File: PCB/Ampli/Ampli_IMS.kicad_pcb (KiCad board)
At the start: 2 copper layers, 65 x 32 mm, 22 parts, among them J1 5227161-3, J2 5227161-3, J3 Conn_01x03_Male, SW1 SS22D0205G2, U1 ADA4625-1, U2 LT1464CS8

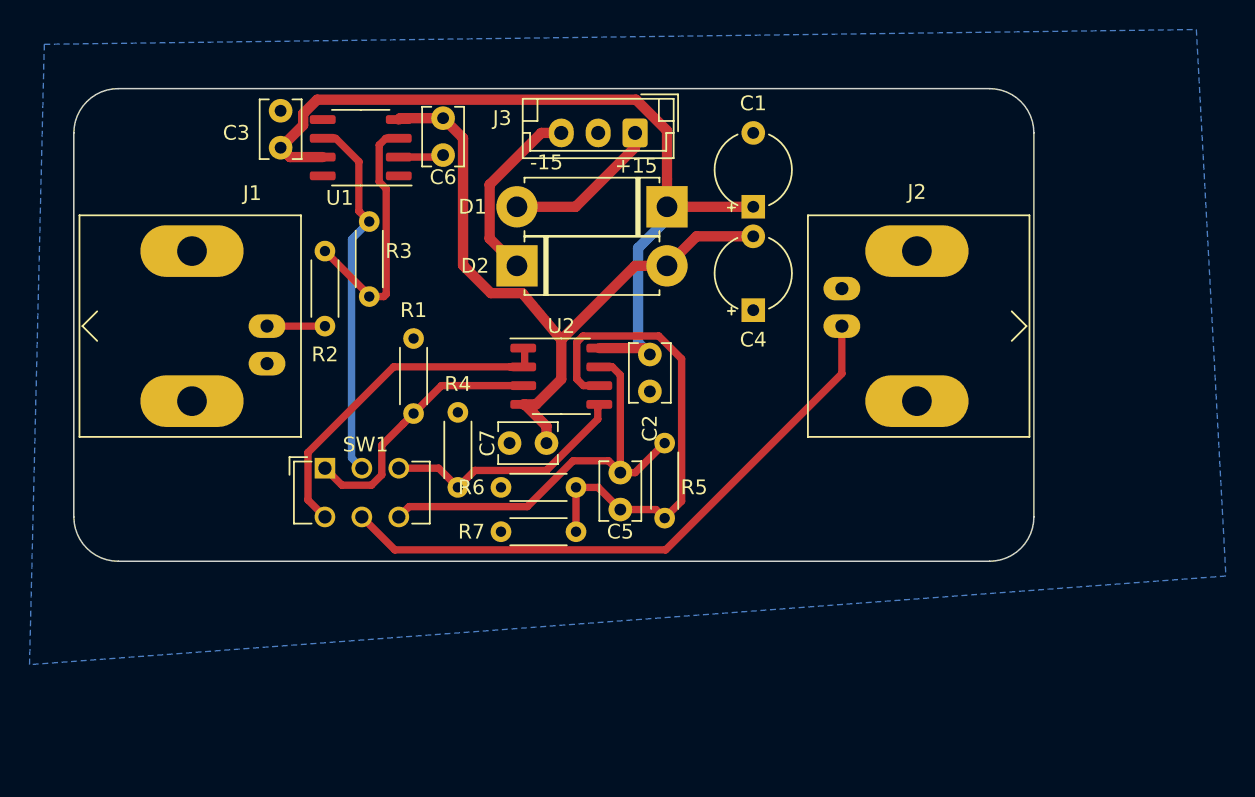
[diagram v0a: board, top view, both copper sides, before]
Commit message: Signal tracks enlarged
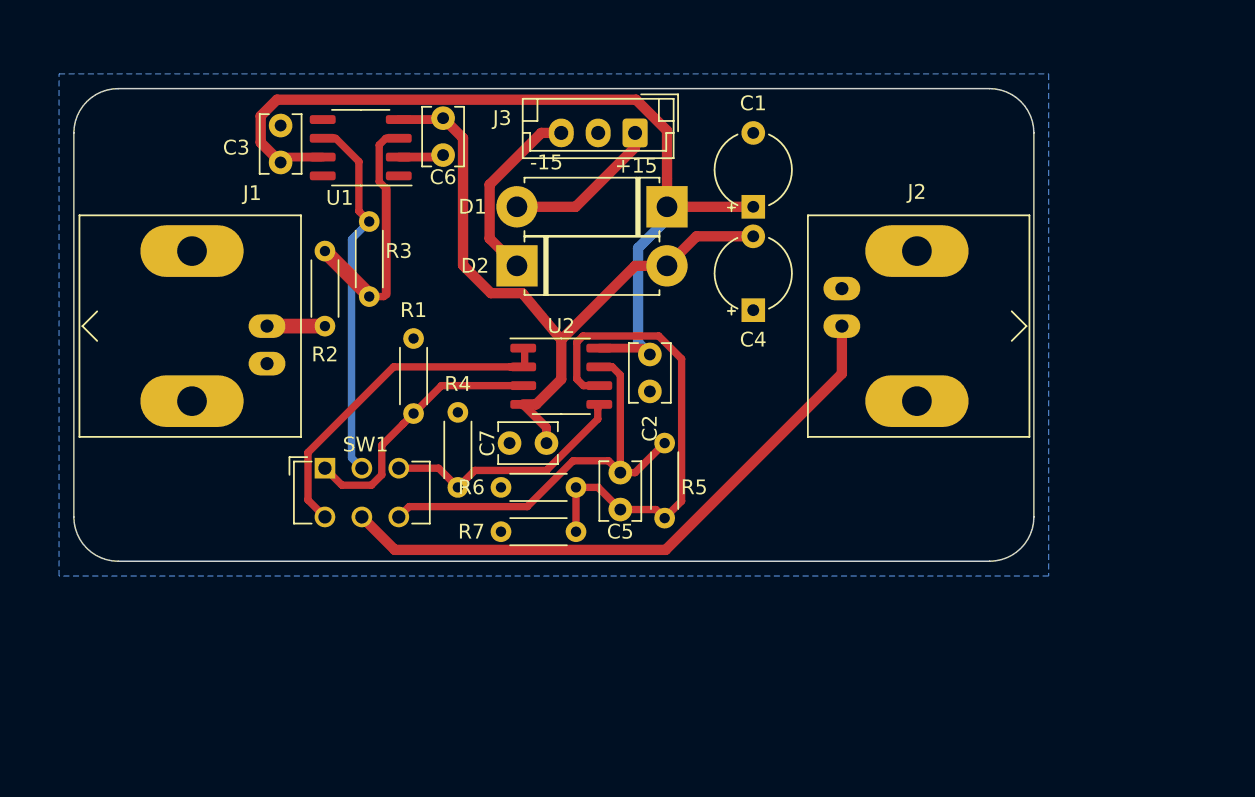
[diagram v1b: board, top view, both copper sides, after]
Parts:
- moved C3 1.00 mm to (32.0, 23.0)
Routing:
- net /+15V: track 57.7 -> 61.3 mm
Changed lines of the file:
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@@
     (user_trace_width 0.4)
     (user_trace_width 0.5)
+    (user_trace_width 0.6)
     (user_trace_width 0.7)
+    (user_trace_width 1)
     (trace_clearance 0.2)
     (zone_clearance 0.508)
@@
   )
   (module Capacitor_THT:C_Disc_D3.8mm_W2.6mm_P2.50mm (layer F.Cu)
-    (at 32 22 90)
+    (at 32 23 90)
     (descr "C, Disc series, Radial, pin pitch=2.50mm, , diameter*width=3.8*2.6mm^2, Capacitor, http://www.vishay.com/docs/45233/krseries.pdf")
     (tags "C Disc series Radial pin pitch 2.50mm  diameter 3.8mm width 2.6mm Capacitor")
@@
   (gr_line (start 21 50) (end 80 50) (layer Edge.Cuts) (width 0.1))
   (segment (start 42.865 22.635) (end 43 22.5) (width 0.5) (layer F.Cu) (net 1))
-  (segment (start 40 22.635) (end 42.865 22.635) (width 0.5) (layer F.Cu) (net 1))
-  (segment (start 32.635 22.635) (end 32 22) (width 0.7) (layer F.Cu) (net 2))
-  (segment (start 34.85 22.635) (end 32.635 22.635) (width 0.7) (layer F.Cu) (net 2))
+  (segment (start 40 22.635) (end 42.865 22.635) (width 0.6) (layer F.Cu) (net 1))
   (segment (start 58.16 26) (end 64 26) (width 0.7) (layer F.Cu) (net 2))
   (segment (start 56.200001 28.799999) (end 58.16 26.84) (width 0.7) (layer B.Cu) (net 2))
@@
   (segment (start 58.16 26.84) (end 58.16 26) (width 0.7) (layer B.Cu) (net 2))
   (segment (start 57 36) (end 56.200001 35.200001) (width 0.7) (layer B.Cu) (net 2))
+  (segment (start 56.57 35.57) (end 57 36) (width 0.5) (layer F.Cu) (net 2))
+  (segment (start 53.575 35.57) (end 56.57 35.57) (width 0.6) (layer F.Cu) (net 2))
+  (segment (start 32.365 22.635) (end 32 23) (width 0.6) (layer F.Cu) (net 2))
+  (segment (start 34.85 22.635) (end 32.365 22.635) (width 0.6) (layer F.Cu) (net 2))
   (segment (start 58.16 24.1) (end 58.16 26) (width 0.7) (layer F.Cu) (net 2))
+  (segment (start 56.064965 18.749999) (end 58.16 20.845034) (width 0.7) (layer F.Cu) (net 2))
+  (segment (start 30.649999 19.851999) (end 31.751999 18.749999) (width 0.7) (layer F.Cu) (net 2))
   (segment (start 58.16 20.845034) (end 58.16 24.1) (width 0.7) (layer F.Cu) (net 2))
-  (segment (start 56.064965 18.749999) (end 58.16 20.845034) (width 0.7) (layer F.Cu) (net 2))
-  (segment (start 34.471457 18.749999) (end 56.064965 18.749999) (width 0.7) (layer F.Cu) (net 2))
-  (segment (start 33.52499 19.696466) (end 34.471457 18.749999) (width 0.7) (layer F.Cu) (net 2))
-  (segment (start 33.52499 20.47501) (end 33.52499 19.696466) (width 0.7) (layer F.Cu) (net 2))
-  (segment (start 32 22) (end 33.52499 20.47501) (width 0.7) (layer F.Cu) (net 2))
-  (segment (start 56.57 35.57) (end 57 36) (width 0.7) (layer F.Cu) (net 2))
-  (segment (start 53.575 35.57) (end 56.57 35.57) (width 0.7) (layer F.Cu) (net 2))
-  (segment (start 50 40.855) (end 48.525 39.38) (width 0.7) (layer F.Cu) (net 3))
-  (segment (start 50 42) (end 50 40.855) (width 0.7) (layer F.Cu) (net 3))
-  (segment (start 40.095 20) (end 40 20.095) (width 0.7) (layer F.Cu) (net 3))
-  (segment (start 43 20) (end 40.095 20) (width 0.7) (layer F.Cu) (net 3))
+  (segment (start 30.649999 21.649999) (end 30.649999 19.851999) (width 0.7) (layer F.Cu) (net 2))
+  (segment (start 31.751999 18.749999) (end 56.064965 18.749999) (width 0.7) (layer F.Cu) (net 2))
+  (segment (start 32 23) (end 30.649999 21.649999) (width 0.7) (layer F.Cu) (net 2))
   (segment (start 60.16 28) (end 64 28) (width 0.7) (layer F.Cu) (net 3))
   (segment (start 58.16 30) (end 60.16 28) (width 0.7) (layer F.Cu) (net 3))
@@
   (segment (start 44.350001 21.350001) (end 44.350001 29.960003) (width 0.7) (layer F.Cu) (net 3))
   (segment (start 43 20) (end 44.350001 21.350001) (width 0.7) (layer F.Cu) (net 3))
+  (segment (start 42.905 20.095) (end 43 20) (width 0.5) (layer F.Cu) (net 3))
+  (segment (start 40 20.095) (end 42.905 20.095) (width 0.6) (layer F.Cu) (net 3))
+  (segment (start 50 40.955) (end 48.425 39.38) (width 0.6) (layer F.Cu) (net 3))
+  (segment (start 50 42) (end 50 40.955) (width 0.6) (layer F.Cu) (net 3))
   (segment (start 52 48) (end 52 45) (width 0.5) (layer F.Cu) (net 4))
   (segment (start 53.5 45) (end 55 46.5) (width 0.5) (layer F.Cu) (net 4))
@@
   (segment (start 48 30) (end 46.149999 28.149999) (width 0.7) (layer F.Cu) (net 7))
   (segment (start 31.24 33.92) (end 31.08 34.08) (width 0.5) (layer F.Cu) (net 8))
-  (segment (start 35 34.08) (end 31.08 34.08) (width 0.5) (layer F.Cu) (net 8))
-  (segment (start 70 37.3) (end 70 34.08) (width 0.5) (layer F.Cu) (net 9))
-  (segment (start 39.730001 49.230001) (end 58.069999 49.230001) (width 0.5) (layer F.Cu) (net 9))
-  (segment (start 58.069999 49.230001) (end 70 37.3) (width 0.5) (layer F.Cu) (net 9))
-  (segment (start 37.5 47) (end 39.730001 49.230001) (width 0.5) (layer F.Cu) (net 9))
+  (segment (start 35 34.08) (end 31.08 34.08) (width 1) (layer F.Cu) (net 8))
+  (segment (start 70 37.3) (end 70 34.08) (width 0.7) (layer F.Cu) (net 9))
+  (segment (start 39.730001 49.230001) (end 58.069999 49.230001) (width 0.7) (layer F.Cu) (net 9))
+  (segment (start 58.069999 49.230001) (end 70 37.3) (width 0.7) (layer F.Cu) (net 9))
+  (segment (start 37.5 47) (end 39.730001 49.230001) (width 0.7) (layer F.Cu) (net 9))
   (segment (start 40.300001 40.699999) (end 41 40) (width 0.5) (layer F.Cu) (net 10))
   (segment (start 38.849999 42.150001) (end 40.300001 40.699999) (width 0.5) (layer F.Cu) (net 10))
@@
   (segment (start 42.89 38.11) (end 48.525 38.11) (width 0.5) (layer F.Cu) (net 10))
   (segment (start 41 40) (end 42.89 38.11) (width 0.5) (layer F.Cu) (net 10))
-  (segment (start 38 32) (end 35 29) (width 0.5) (layer F.Cu) (net 11))
+  (segment (start 38 32) (end 35 29) (width 1) (layer F.Cu) (net 11))
   (segment (start 38 32.08) (end 38 32) (width 0.5) (layer F.Cu) (net 11))
   (segment (start 39.125 21.365) (end 40 21.365) (width 0.5) (layer F.Cu) (net 11))
   (segment (start 38.67499 21.81501) (end 39.125 21.365) (width 0.5) (layer F.Cu) (net 11))
   (segment (start 39.150001 24.778545) (end 38.67499 24.303534) (width 0.5) (layer F.Cu) (net 11))
-  (segment (start 39.150001 31.919948) (end 39.150001 24.778545) (width 0.5) (layer F.Cu) (net 11))
+  (segment (start 39.150001 31.919948) (end 39.150001 24.778545) (width 0.6) (layer F.Cu) (net 11))
   (segment (start 38.989949 32.08) (end 39.150001 31.919948) (width 0.5) (layer F.Cu) (net 11))
   (segment (start 38.67499 24.303534) (end 38.67499 21.81501) (width 0.5) (layer F.Cu) (net 11))
@@
     (polygon
       (pts
-        (xy 96 51) (xy 15 57) (xy 16 15) (xy 94 14)
+        (xy 84 51) (xy 17 51) (xy 17 17) (xy 84 17)
       )
     )

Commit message: low noise pcb design
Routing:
- net Net-(R3-Pad1): track 24.9 -> 29.1 mm
- net Net-(SW1-Pad4): track 23.2 -> 20.1 mm, vias 0 -> 1
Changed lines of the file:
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@@
     (thickness 1.6)
     (drawings 10)
-    (tracks 107)
+    (tracks 114)
     (zones 0)
     (modules 22)
@@
   )
   (setup
-    (last_trace_width 0.7)
+    (last_trace_width 0.6)
     (user_trace_width 0.4)
     (user_trace_width 0.5)
@@
     (add_net "Net-(U1-Pad8)")
   )
+  (module Resistor_THT:R_Axial_DIN0204_L3.6mm_D1.6mm_P5.08mm_Horizontal (layer F.Cu)
+    (at 38 27 270)
+    (descr "Resistor, Axial_DIN0204 series, Axial, Horizontal, pin pitch=5.08mm, 0.167W, length*diameter=3.6*1.6mm^2, http://cdn-reichelt.de/documents/datenblatt/B400/1_4W%23YAG.pdf")
+    (tags "Resistor Axial_DIN0204 series Axial Horizontal pin pitch 5.08mm 0.167W length 3.6mm diameter 1.6mm")
+    (fp_text reference R3 (at 2 -2 180) (layer F.SilkS)
+      (effects (font (size 1 1) (thickness 0.15)))
+    )
+    (fp_text value "100M 1/4W" (at 2.54 1.92 90) (layer F.Fab)
+      (effects (font (size 1 1) (thickness 0.15)))
+    )
+    (fp_text user %R (at 2.54 0 90) (layer F.Fab)
+      (effects (font (size 0.72 0.72) (thickness 0.108)))
+    )
+    (fp_line (start 6.03 -1.05) (end -0.95 -1.05) (layer F.CrtYd) (width 0.05))
+    (fp_line (start 6.03 1.05) (end 6.03 -1.05) (layer F.CrtYd) (width 0.05))
+    (fp_line (start -0.95 1.05) (end 6.03 1.05) (layer F.CrtYd) (width 0.05))
+    (fp_line (start -0.95 -1.05) (end -0.95 1.05) (layer F.CrtYd) (width 0.05))
+    (fp_line (start 0.62 0.92) (end 4.46 0.92) (layer F.SilkS) (width 0.12))
+    (fp_line (start 0.62 -0.92) (end 4.46 -0.92) (layer F.SilkS) (width 0.12))
+    (fp_line (start 5.08 0) (end 4.34 0) (layer F.Fab) (width 0.1))
+    (fp_line (start 0 0) (end 0.74 0) (layer F.Fab) (width 0.1))
+    (fp_line (start 4.34 -0.8) (end 0.74 -0.8) (layer F.Fab) (width 0.1))
+    (fp_line (start 4.34 0.8) (end 4.34 -0.8) (layer F.Fab) (width 0.1))
+    (fp_line (start 0.74 0.8) (end 4.34 0.8) (layer F.Fab) (width 0.1))
+    (fp_line (start 0.74 -0.8) (end 0.74 0.8) (layer F.Fab) (width 0.1))
+    (pad 2 thru_hole oval (at 5.08 0 270) (size 1.4 1.4) (drill 0.7) (layers *.Cu *.Mask)
+      (net 11 "Net-(R2-Pad1)"))
+    (pad 1 thru_hole circle (at 0 0 270) (size 1.4 1.4) (drill 0.7) (layers *.Cu *.Mask)
+      (net 12 "Net-(R3-Pad1)"))
+    (model ${KISYS3DMOD}/Resistor_THT.3dshapes/R_Axial_DIN0204_L3.6mm_D1.6mm_P5.08mm_Horizontal.wrl
+      (at (xyz 0 0 0))
+      (scale (xyz 1 1 1))
+      (rotate (xyz 0 0 0))
+    )
+  )
   (module Capacitor_THT:CP_Radial_Tantal_D5.0mm_P5.00mm (layer F.Cu)
     (at 64 33 90)
@@
     (pad 1 thru_hole circle (at 0 0 90) (size 1.4 1.4) (drill 0.7) (layers *.Cu *.Mask)
       (net 13 "Net-(R4-Pad1)"))
-    (model ${KISYS3DMOD}/Resistor_THT.3dshapes/R_Axial_DIN0204_L3.6mm_D1.6mm_P5.08mm_Horizontal.wrl
-      (at (xyz 0 0 0))
-      (scale (xyz 1 1 1))
-      (rotate (xyz 0 0 0))
-    )
-  )
-  (module Resistor_THT:R_Axial_DIN0204_L3.6mm_D1.6mm_P5.08mm_Horizontal (layer F.Cu)
-    (at 38 27 270)
-    (descr "Resistor, Axial_DIN0204 series, Axial, Horizontal, pin pitch=5.08mm, 0.167W, length*diameter=3.6*1.6mm^2, http://cdn-reichelt.de/documents/datenblatt/B400/1_4W%23YAG.pdf")
-    (tags "Resistor Axial_DIN0204 series Axial Horizontal pin pitch 5.08mm 0.167W length 3.6mm diameter 1.6mm")
-    (fp_text reference R3 (at 2 -2 180) (layer F.SilkS)
-      (effects (font (size 1 1) (thickness 0.15)))
-    )
-    (fp_text value "100M 1/4W" (at 2.54 1.92 90) (layer F.Fab)
-      (effects (font (size 1 1) (thickness 0.15)))
-    )
-    (fp_text user %R (at 2.54 0 90) (layer F.Fab)
-      (effects (font (size 0.72 0.72) (thickness 0.108)))
-    )
-    (fp_line (start 6.03 -1.05) (end -0.95 -1.05) (layer F.CrtYd) (width 0.05))
-    (fp_line (start 6.03 1.05) (end 6.03 -1.05) (layer F.CrtYd) (width 0.05))
-    (fp_line (start -0.95 1.05) (end 6.03 1.05) (layer F.CrtYd) (width 0.05))
-    (fp_line (start -0.95 -1.05) (end -0.95 1.05) (layer F.CrtYd) (width 0.05))
-    (fp_line (start 0.62 0.92) (end 4.46 0.92) (layer F.SilkS) (width 0.12))
-    (fp_line (start 0.62 -0.92) (end 4.46 -0.92) (layer F.SilkS) (width 0.12))
-    (fp_line (start 5.08 0) (end 4.34 0) (layer F.Fab) (width 0.1))
-    (fp_line (start 0 0) (end 0.74 0) (layer F.Fab) (width 0.1))
-    (fp_line (start 4.34 -0.8) (end 0.74 -0.8) (layer F.Fab) (width 0.1))
-    (fp_line (start 4.34 0.8) (end 4.34 -0.8) (layer F.Fab) (width 0.1))
-    (fp_line (start 0.74 0.8) (end 4.34 0.8) (layer F.Fab) (width 0.1))
-    (fp_line (start 0.74 -0.8) (end 0.74 0.8) (layer F.Fab) (width 0.1))
-    (pad 2 thru_hole oval (at 5.08 0 270) (size 1.4 1.4) (drill 0.7) (layers *.Cu *.Mask)
-      (net 11 "Net-(R2-Pad1)"))
-    (pad 1 thru_hole circle (at 0 0 270) (size 1.4 1.4) (drill 0.7) (layers *.Cu *.Mask)
-      (net 12 "Net-(R3-Pad1)"))
     (model ${KISYS3DMOD}/Resistor_THT.3dshapes/R_Axial_DIN0204_L3.6mm_D1.6mm_P5.08mm_Horizontal.wrl
       (at (xyz 0 0 0))
@@
   (segment (start 38.67499 24.303534) (end 38.67499 21.81501) (width 0.5) (layer F.Cu) (net 11))
   (segment (start 38 32.08) (end 38.989949 32.08) (width 0.5) (layer F.Cu) (net 11))
-  (segment (start 35.725 21.365) (end 34.85 21.365) (width 0.5) (layer F.Cu) (net 12))
-  (segment (start 37.300001 26.300001) (end 37.300001 22.940001) (width 0.5) (layer F.Cu) (net 12))
-  (segment (start 37.300001 22.940001) (end 35.725 21.365) (width 0.5) (layer F.Cu) (net 12))
-  (segment (start 38 27) (end 37.300001 26.300001) (width 0.5) (layer F.Cu) (net 12))
-  (segment (start 36.800001 43.000001) (end 37.5 43.7) (width 0.5) (layer B.Cu) (net 12))
-  (segment (start 36.800001 28.199999) (end 36.800001 43.000001) (width 0.5) (layer B.Cu) (net 12))
-  (segment (start 38 27) (end 36.800001 28.199999) (width 0.5) (layer B.Cu) (net 12))
+  (segment (start 37.300001 26.300001) (end 38 27) (width 0.7) (layer F.Cu) (net 12))
+  (segment (start 37.300001 22.940001) (end 37.300001 26.300001) (width 0.7) (layer F.Cu) (net 12))
+  (segment (start 35.725 21.365) (end 37.300001 22.940001) (width 0.7) (layer F.Cu) (net 12))
+  (segment (start 34.85 21.365) (end 35.725 21.365) (width 0.7) (layer F.Cu) (net 12))
+  (segment (start 37.010051 27) (end 38 27) (width 0.7) (layer F.Cu) (net 12))
+  (segment (start 33.799999 28.423999) (end 35.223998 27) (width 0.7) (layer F.Cu) (net 12))
+  (segment (start 35.223998 27) (end 37.010051 27) (width 0.7) (layer F.Cu) (net 12))
+  (segment (start 33.799999 29.576001) (end 33.799999 28.423999) (width 0.7) (layer F.Cu) (net 12))
+  (segment (start 36.800001 32.576003) (end 33.799999 29.576001) (width 0.7) (layer F.Cu) (net 12))
+  (segment (start 36.800001 43.000001) (end 36.800001 32.576003) (width 0.7) (layer F.Cu) (net 12))
+  (segment (start 37.5 43.7) (end 36.800001 43.000001) (width 0.7) (layer F.Cu) (net 12))
   (segment (start 42.7 43.7) (end 44 45) (width 0.5) (layer F.Cu) (net 13))
   (segment (start 40 43.7) (end 42.7 43.7) (width 0.5) (layer F.Cu) (net 13))
@@
   (segment (start 53.475 40.375002) (end 53.475 39.68) (width 0.5) (layer F.Cu) (net 13))
   (segment (start 44 45) (end 45.150001 43.849999) (width 0.5) (layer F.Cu) (net 13))
-  (segment (start 39.649998 36.84) (end 47.55 36.84) (width 0.5) (layer F.Cu) (net 14))
-  (segment (start 33.849999 42.639999) (end 39.649998 36.84) (width 0.5) (layer F.Cu) (net 14))
-  (segment (start 47.55 36.84) (end 48.525 36.84) (width 0.5) (layer F.Cu) (net 14))
-  (segment (start 33.849999 45.849999) (end 33.849999 42.639999) (width 0.5) (layer F.Cu) (net 14))
-  (segment (start 35 47) (end 33.849999 45.849999) (width 0.5) (layer F.Cu) (net 14))
   (segment (start 48.525 36.84) (end 48.525 35.57) (width 0.5) (layer F.Cu) (net 14))
+  (segment (start 46.7 36.9) (end 46.7 36.9) (width 0.6) (layer B.Cu) (net 14))
+  (segment (start 36.200001 45.799999) (end 35 47) (width 0.6) (layer B.Cu) (net 14))
+  (segment (start 39.896003 45.799999) (end 36.200001 45.799999) (width 0.6) (layer B.Cu) (net 14))
+  (segment (start 46.7 38.996002) (end 39.896003 45.799999) (width 0.6) (layer B.Cu) (net 14))
+  (segment (start 46.7 36.9) (end 46.7 38.996002) (width 0.6) (layer B.Cu) (net 14))
+  (via (at 46.7 36.9) (size 0.8) (drill 0.4) (layers F.Cu B.Cu) (net 14))
+  (segment (start 48.365 36.9) (end 48.425 36.84) (width 0.6) (layer F.Cu) (net 14))
+  (segment (start 46.7 36.9) (end 48.365 36.9) (width 0.6) (layer F.Cu) (net 14))
   (zone (net 1) (net_name GND) (layer B.Cu) (hatch edge 0.508)
     (connect_pads (clearance 0.508))
@@
       )
     )
+  )
+  (zone (net 0) (net_name "") (layer B.Cu) (hatch edge 0.508)
+    (connect_pads (clearance 0.508))
+    (min_thickness 0.254)
+    (keepout (tracks allowed) (vias allowed) (copperpour not_allowed))
+    (fill (arc_segments 32) (thermal_gap 0.508) (thermal_bridge_width 0.508))
+    (polygon
+      (pts
+        (xy 41.1 21.9) (xy 39.1 21.9) (xy 39.1 22.1) (xy 39.1 24.125) (xy 39.6 24.675)
+        (xy 39.6 32.4) (xy 38.5 32.4) (xy 38.5 31.8) (xy 38.7 31.8) (xy 38.7 24.9)
+        (xy 38.2 24.4) (xy 38.2 21.55) (xy 38.9 20.85) (xy 41.1 20.8)
+      )
+    )
